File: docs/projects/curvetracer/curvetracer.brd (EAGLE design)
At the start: 58.1 x 52.1 mm, 9 parts, among them IC2 MC33201

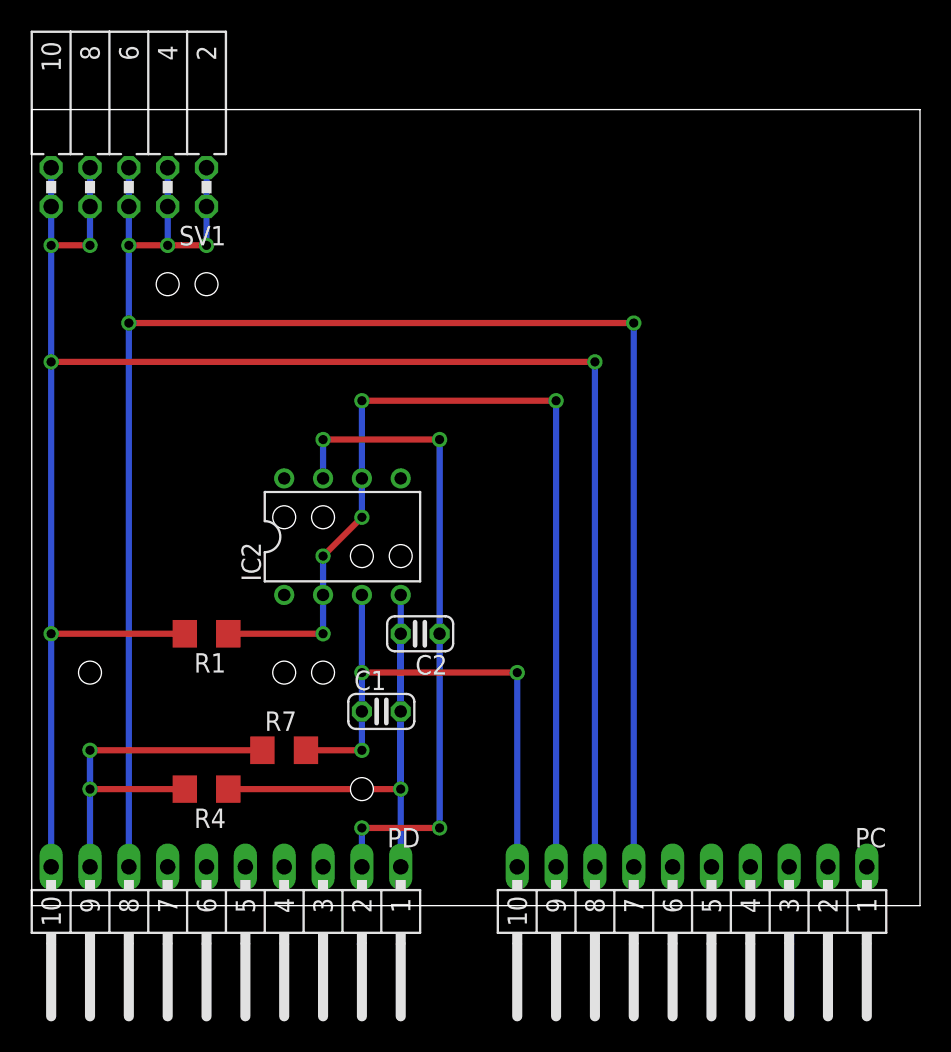
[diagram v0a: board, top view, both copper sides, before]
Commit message: support for voltagetransfer
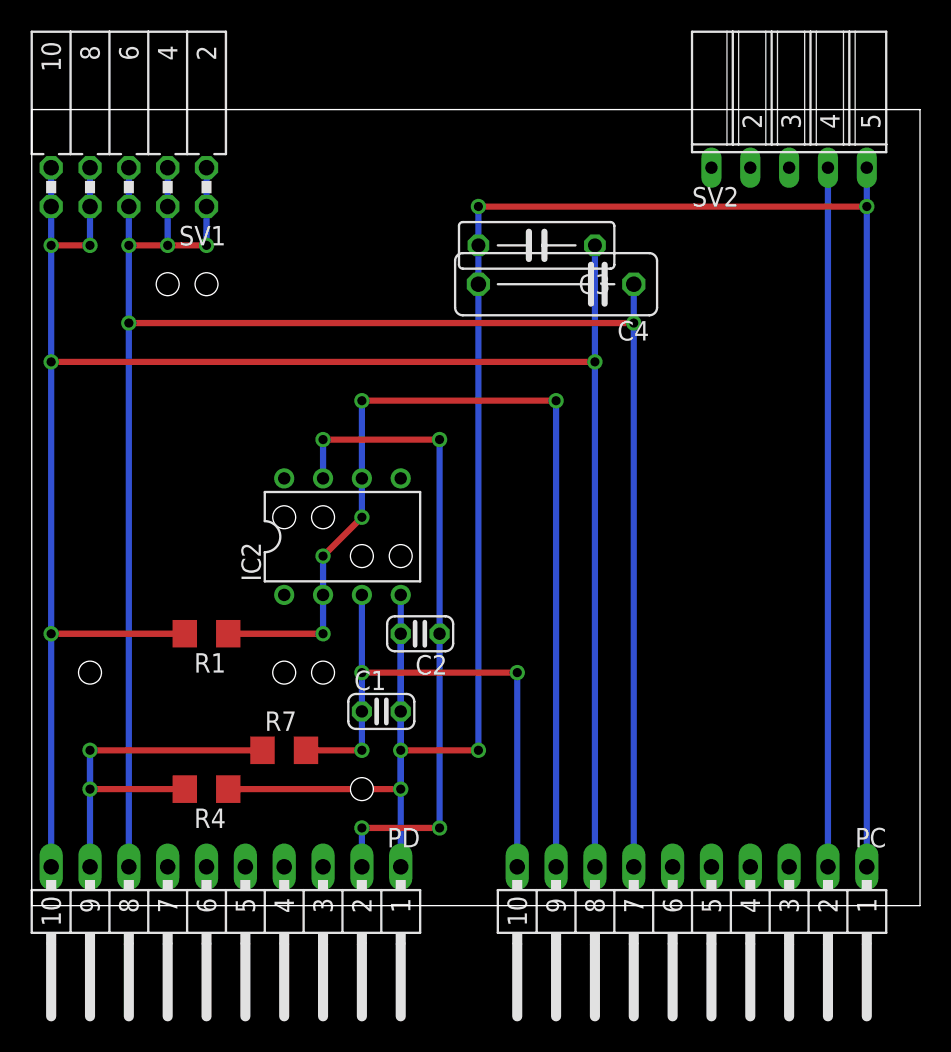
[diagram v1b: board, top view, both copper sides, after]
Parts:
- added C3: 100n, rcl:C075-032X103
- added C4: 100n, rcl:C102-043X133
- added SV2: (no value), con-lsta:FE05W
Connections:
- new net N$1: PC.2, SV2.4
- net A2D8: now also C3.1
- net A3D10: now also C4.1
- net GND: now also C3.2, C4.2, PC.1, SV2.5
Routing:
- net GND: track 49.4 -> 151.0 mm, vias 1 -> 5
- net N$1: track 0.00 -> 45.7 mm
- net A2D8: track 130.7 -> 138.3 mm
- net A3D10: track 129.5 -> 132.1 mm
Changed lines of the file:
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@@
 <?xml version="1.0" encoding="utf-8"?>
 <!DOCTYPE eagle SYSTEM "eagle.dtd">
-<eagle version="6.2">
+<eagle version="6.4">
 <drawing>
 <settings>
@@
 <wire x1="31.75" y1="40.64" x2="31.75" y2="50.8" width="0.4064" layer="111"/>
 <wire x1="31.75" y1="50.8" x2="36.83" y2="50.8" width="0.4064" layer="111"/>
-<wire x1="38.1" y1="50.8" x2="45.72" y2="50.8" width="0.4064" layer="111"/>
+<wire x1="36.83" y1="50.8" x2="45.72" y2="50.8" width="0.4064" layer="111"/>
 <wire x1="36.83" y1="40.64" x2="36.83" y2="50.8" width="0.4064" layer="111"/>
-<wire x1="36.83" y1="50.8" x2="38.1" y2="50.8" width="0.4064" layer="111"/>
-<text x="45.72" y="40.64" size="3.81" layer="111">CURVE TRACER</text>
+<text x="76.2" y="35.56" size="2.54" layer="111" rot="R270">CURVE TRACER</text>
 <hole x="35.56" y="15.24" drill="1.5"/>
 <hole x="40.64" y="40.64" drill="1.5"/>
@@
 </class>
 </classes>
-<designrules>
+<designrules name="default">
 <description language="de">&lt;b&gt;EAGLE Design Rules&lt;/b&gt;
 &lt;p&gt;
@@
 <element name="IC2" library="linear" package="DIL08" value="MC33201" x="52.07" y="24.13"/>
 <element name="C2" library="rcl" package="C025-024X044" value="100n" x="57.15" y="17.78" rot="R180"/>
+<element name="SV2" library="con-lsta" package="FE05W" value="" x="81.28" y="48.26">
+<attribute name="OC_NEWARK" value="unknown" x="81.28" y="48.26" size="1.778" layer="27" display="off"/>
+<attribute name="MPN" value="" x="81.28" y="48.26" size="1.778" layer="27" display="off"/>
+<attribute name="MF" value="" x="81.28" y="48.26" size="1.778" layer="27" display="off"/>
+<attribute name="OC_FARNELL" value="unknown" x="81.28" y="48.26" size="1.778" layer="27" display="off"/>
+</element>
+<element name="C3" library="rcl" package="C075-032X103" value="100n" x="64.77" y="43.18" rot="R180"/>
+<element name="C4" library="rcl" package="C102-043X133" value="100n" x="66.04" y="40.64" rot="R180"/>
 </elements>
 <signals>
@@
 <contactref element="IC2" pad="4"/>
 <contactref element="C2" pad="2"/>
-<wire x1="55.88" y1="7.62" x2="55.88" y2="17.78" width="0.4064" layer="16"/>
-<wire x1="55.88" y1="17.78" x2="55.88" y2="2.54" width="0.4064" layer="16"/>
-<wire x1="55.88" y1="7.62" x2="55.88" y2="12.7" width="0.4064" layer="16"/>
+<wire x1="55.88" y1="17.78" x2="55.88" y2="10.16" width="0.4064" layer="16"/>
+<wire x1="55.88" y1="10.16" x2="55.88" y2="2.54" width="0.4064" layer="16"/>
+<wire x1="55.88" y1="7.62" x2="55.88" y2="10.16" width="0.4064" layer="16"/>
+<wire x1="55.88" y1="10.16" x2="55.88" y2="12.7" width="0.4064" layer="16"/>
 <wire x1="55.88" y1="12.7" x2="55.88" y2="20.32" width="0.4064" layer="16"/>
 <wire x1="44.602" y1="7.62" x2="55.88" y2="7.62" width="0.4064" layer="1"/>
 <via x="55.88" y="7.62" extent="1-16" drill="0.6" shape="square"/>
+<contactref element="C3" pad="2"/>
+<contactref element="C4" pad="2"/>
+<via x="55.88" y="10.16" extent="1-16" drill="0.6" shape="square"/>
+<wire x1="55.88" y1="10.16" x2="60.96" y2="10.16" width="0.4064" layer="1"/>
+<via x="60.96" y="10.16" extent="1-16" drill="0.6" shape="square"/>
+<wire x1="60.96" y1="10.16" x2="60.96" y2="40.64" width="0.4064" layer="16"/>
+<wire x1="60.96" y1="40.64" x2="60.96" y2="43.18" width="0.4064" layer="16"/>
+<wire x1="60.96" y1="43.18" x2="60.96" y2="45.72" width="0.4064" layer="16"/>
+<via x="60.96" y="45.72" extent="1-16" drill="0.6" shape="square"/>
+<contactref element="PC" pad="1"/>
+<contactref element="SV2" pad="5"/>
+<wire x1="86.36" y1="2.54" x2="86.36" y2="45.72" width="0.4064" layer="16"/>
+<wire x1="86.36" y1="45.72" x2="86.36" y2="48.26" width="0.4064" layer="16"/>
+<via x="86.36" y="45.72" extent="1-16" drill="0.6" shape="square"/>
+<wire x1="60.96" y1="45.72" x2="86.36" y2="45.72" width="0.4064" layer="1"/>
 </signal>
 <signal name="A2D8">
@@
 <via x="35.56" y="43.18" extent="1-16" drill="0.6" shape="square"/>
 <via x="33.02" y="43.18" extent="1-16" drill="0.6" shape="square"/>
+<contactref element="C3" pad="1"/>
+<wire x1="68.58" y1="35.56" x2="68.58" y2="43.18" width="0.4064" layer="16"/>
 </signal>
 <signal name="D9">
@@
 <via x="43.18" y="43.18" extent="1-16" drill="0.6" shape="square"/>
 <via x="38.1" y="43.18" extent="1-16" drill="0.6" shape="square"/>
+<contactref element="C4" pad="1"/>
+<wire x1="71.12" y1="38.1" x2="71.12" y2="40.64" width="0.4064" layer="16"/>
 </signal>
 <signal name="A4D13">
@@
 <contactref element="PD" pad="5"/>
 </signal>
+<signal name="N$1">
+<contactref element="SV2" pad="4"/>
+<contactref element="PC" pad="2"/>
+<wire x1="83.82" y1="48.26" x2="83.82" y2="2.54" width="0.4064" layer="16"/>
+</signal>
 </signals>
